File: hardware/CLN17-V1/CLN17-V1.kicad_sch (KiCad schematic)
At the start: 88 parts, among them IC1 STM32G431CB, J1 Motor, J2 USB_C, J3 CTRL, J4 PWR, J5 CAN, J6 CAN, J7 IO, SW1 SW_Push, SW2 SW_Push, U1 TMC2209, U2 TLE5012B, U4 XC6206, U5 USBLC6-4SC6, U6 USBLC6-4SC6, U7 USBLC6-4SC6, U8 TJA1051, U9 TP6841, Y1 8M

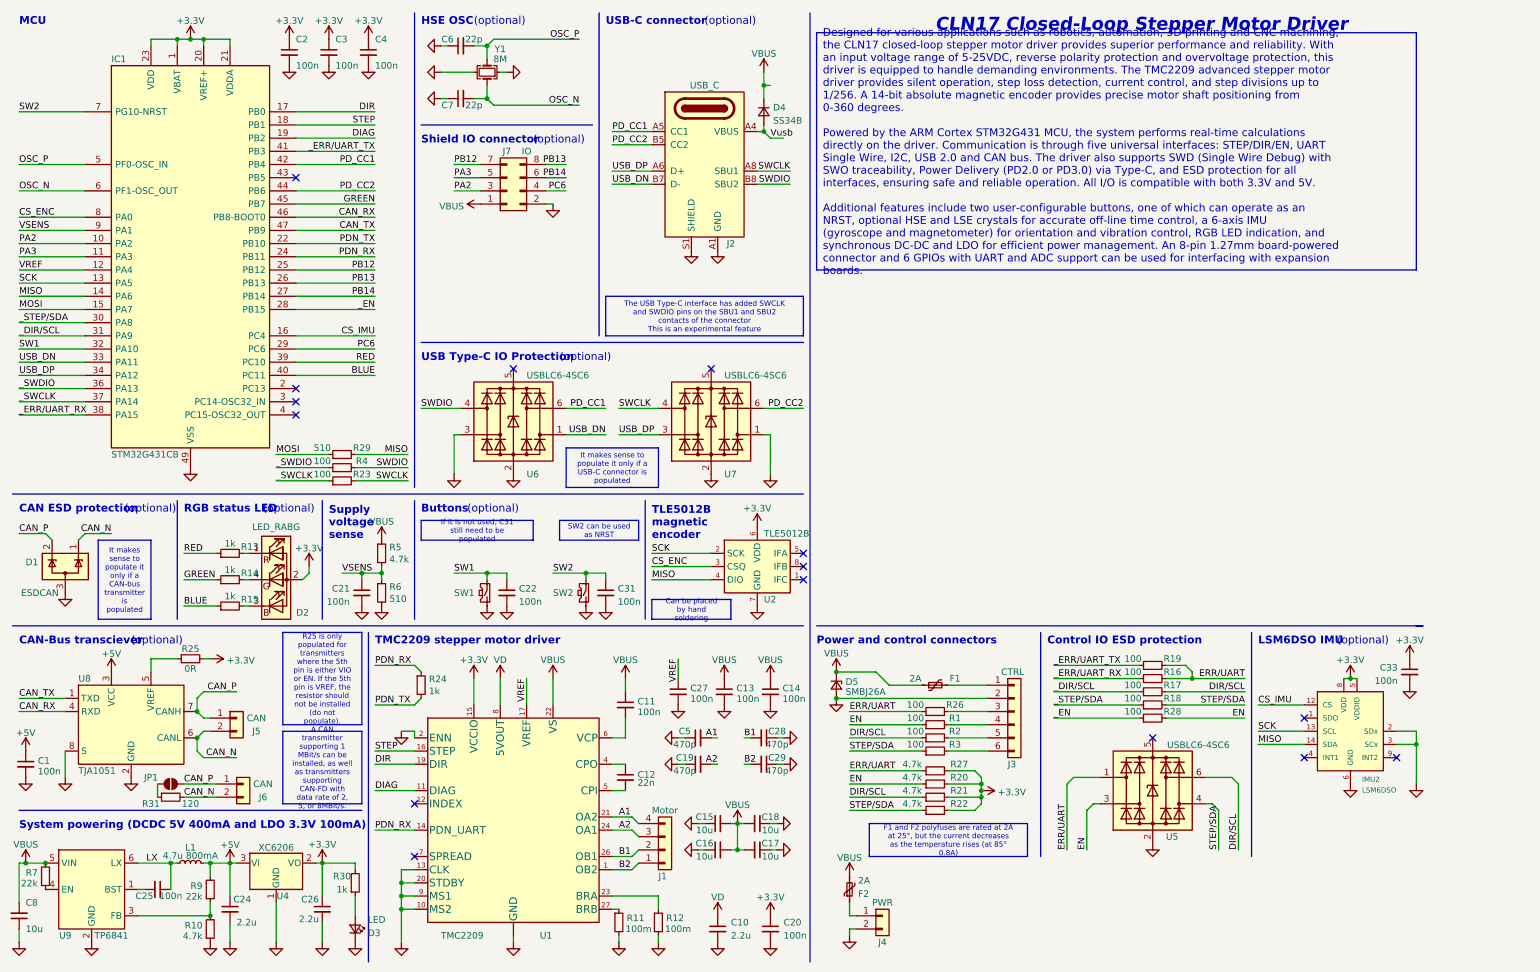
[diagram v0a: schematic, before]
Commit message: V1.1 fixes
- Optimised circuit power supply:
	- Improved power polygon layout;
	- Improved DCDC converter layout
- Improved Type-C compatibility:
	- Added full-featured UCPD interface;
	- Added 5.1k resistors in case UCPD doesn't work
- Optimised components:
	- ESD protection reduced form factor;
	- Correct USB Type-C connector with both CC lines
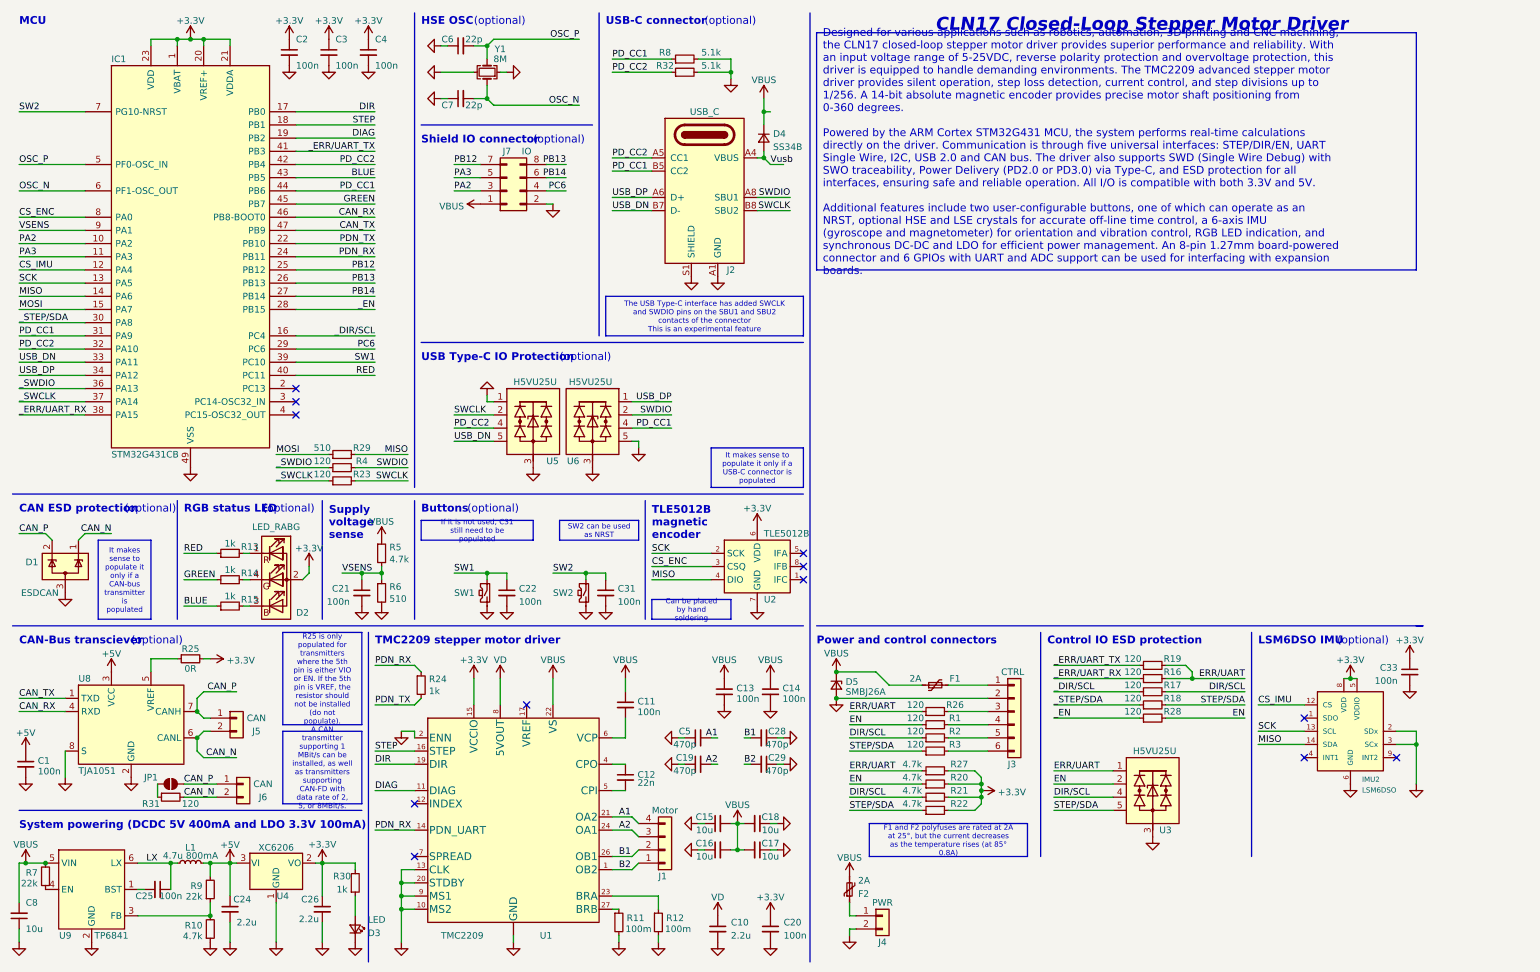
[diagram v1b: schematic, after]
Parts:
- removed C27: 100n, FP_lib:C0402, symbol C_Small
- removed U5, U6, U7: USBLC6-4SC6, FP_lib:SOT-23-6, symbol USBLC6-4SC6
- added R32, R8: 5.1k, FP_lib:R0402, symbol R_Small
- added U3, U5, U6: H5VU25U, FP_lib:DFN-2510, symbol CLN17-V2:USBLC6-4SC6_1
- J2: LCSC Part # C2765186 -> C963413
- R1, R16, R17, R18, R19, R2, R23, R26, R28, R3, R4: value 100 -> 120; LCSC Part # C25076 -> C25079
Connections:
- net BLUE: now also IC1.43 (PB5); no longer IC1.40 (PC11)
- net CS_IMU: now also IC1.12 (PA4); no longer IC1.16 (PC4)
- net DIR/SCL: now also U3.4 (I/O3), U3.7 (I/O3)
- net EN: now also U3.2 (I/O2), U3.9 (I/O2)
- net ERR/UART: now also U3.1 (I/O1), U3.10
- net GND: now also R32.2, R8.2, U3.3 (GND), U3.8 (GND), U5.1 (I/O1), U5.10, U5.3 (GND), U5.8 (GND), U6.3 (GND), U6.5 (I/O4), U6.6 (I/O4), U6.8 (GND)
- net PD_CC1: now also IC1.31 (PA9), IC1.44 (PB6), J2.B5 (CC2), R8.1, U6.4 (I/O3), U6.7 (I/O3); no longer IC1.42 (PB4), J2.A5 (CC1)
- net PD_CC2: now also IC1.32 (PA10), IC1.42 (PB4), J2.A5 (CC1), R32.1, U5.4 (I/O3), U5.7 (I/O3); no longer IC1.44 (PB6), J2.B5 (CC2)
- net RED: now also IC1.40 (PC11); no longer IC1.39 (PC10)
- net STEP/SDA: now also U3.5 (I/O4), U3.6 (I/O4)
- net SW1: now also IC1.39 (PC10); no longer IC1.32 (PA10)
- net SWCLK: now also J2.B8 (SBU2), U5.2 (I/O2), U5.9 (I/O2); no longer J2.A8 (SBU1)
- net SWDIO: now also J2.A8 (SBU1), U6.2 (I/O2), U6.9 (I/O2); no longer J2.B8 (SBU2)
- net USB_DN: now also U5.5 (I/O4), U5.6 (I/O4)
- net USB_DP: now also U6.1 (I/O1), U6.10
- net _DIR/SCL: now also IC1.16 (PC4); no longer IC1.31 (PA9)
- net VREF: no longer names the net of U1.17 (VREF)
- net VREF: no longer IC1.12 (PA4)
- no-connect marks 15 -> 12
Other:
- moved on the sheet: D4, J2
